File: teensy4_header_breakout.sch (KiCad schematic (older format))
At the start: 3 parts, among them J1 Conn_01x14, J2 Conn_01x14, U1 GND-1

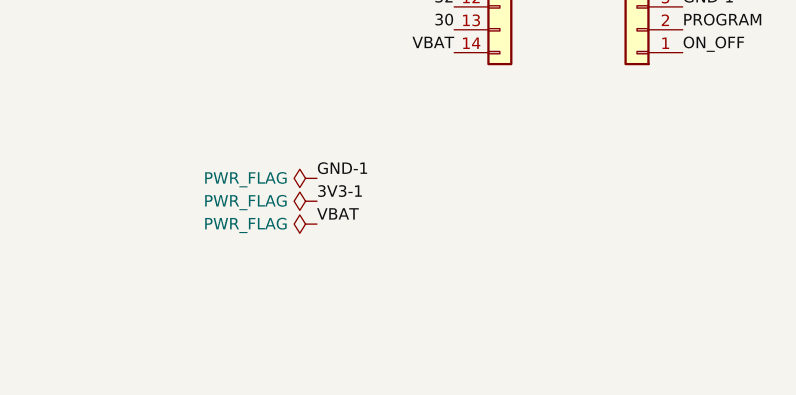
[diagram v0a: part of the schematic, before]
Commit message: Added ground plane and graphics for sidecars
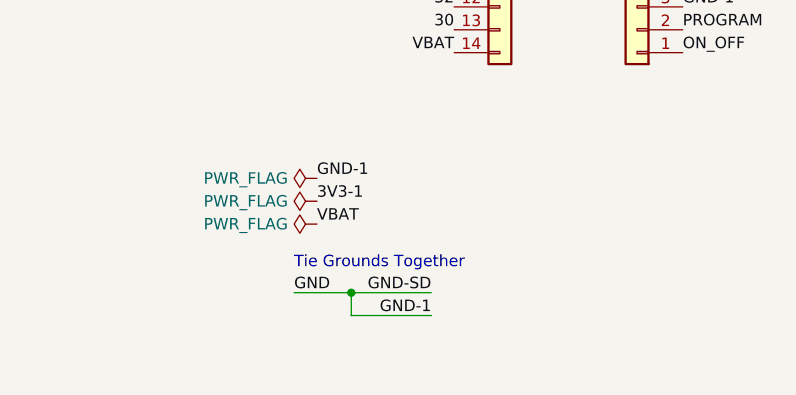
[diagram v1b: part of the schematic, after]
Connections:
- net GND-1 is gone; now on net GND: J2.3 (Pin_3), U1.17 (GND)
- net GND-SD is gone; now on net GND: J1.3 (Pin_3), U1.47 (GND)
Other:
- note added: "Tie Grounds Together"
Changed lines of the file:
@@
 Text Label 6250 5800 0    50   ~ 0
 GND
+Wire Wire Line
+	8550 6050 8200 6050
+Text Label 7950 6050 0    50   ~ 0
+GND
+Text Label 8550 6050 2    50   ~ 0
+GND-SD
+Text Notes 7950 5950 0    50   ~ 0
+Tie Grounds Together
+Wire Wire Line
+	8550 6150 8200 6150
+Wire Wire Line
+	8200 6150 8200 6050
+Connection ~ 8200 6050
+Wire Wire Line
+	8200 6050 7950 6050
+Text Label 8550 6150 2    50   ~ 0
+GND-1
 $EndSCHEMATC

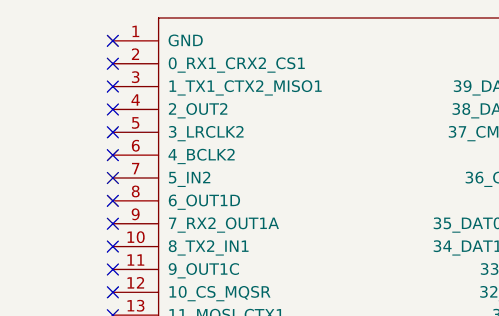
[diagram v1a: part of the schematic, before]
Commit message: Add gnd pin to plane
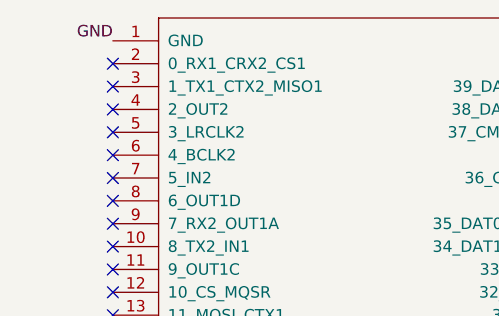
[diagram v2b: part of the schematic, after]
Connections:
- net GND: now also U1.1 (GND)
- no-connect marks 27 -> 26
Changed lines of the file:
@@
 $EndDescr
-$Comp
-L Teensy:Teensy4.0 U1
-U 1 1 5D7811A6
-P 5150 4750
-F 0 "U1" H 5150 3135 50  0000 C CNN
-F 1 "GND-1" H 5150 3226 50  0000 C CNN
-F 2 "Teensy:Teensy40_SMT" H 4750 4950 50  0001 C CNN
-F 3 "" H 4750 4950 50  0001 C CNN
-	1    5150 4750
-	1    0    0    -1
-$EndComp
 $Comp
 L Connector_Generic:Conn_01x14 J2
@@
 	-1   0    0    1
 $EndComp
-NoConn ~ 4050 3400
 NoConn ~ 4050 3500
 NoConn ~ 4050 3600
@@
 Text Label 8550 6150 2    50   ~ 0
 GND-1
+$Comp
+L Teensy:Teensy4.0 U1
+U 1 1 5D7811A6
+P 5150 4750
+F 0 "U1" H 5150 3135 50  0000 C CNN
+F 1 "GND-1" H 5150 3226 50  0000 C CNN
+F 2 "Teensy:Teensy40_SMT" H 4750 4950 50  0001 C CNN
+F 3 "" H 4750 4950 50  0001 C CNN
+	1    5150 4750
+	1    0    0    -1
+$EndComp
+Text Label 4050 3400 2    50   ~ 0
+GND
 $EndSCHEMATC
